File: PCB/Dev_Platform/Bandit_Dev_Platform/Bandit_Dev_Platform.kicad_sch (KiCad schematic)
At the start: 136 parts, among them J1 Conn_01x03_Pin, J10 Conn_01x05_Pin, J11 Conn_01x05_Pin, J2 SMA, J3 Conn_01x05_Pin, J4 Conn_01x05_Pin, J5 BNC, J6 BNC, J7 SMA, J8 Conn_01x05_Pin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

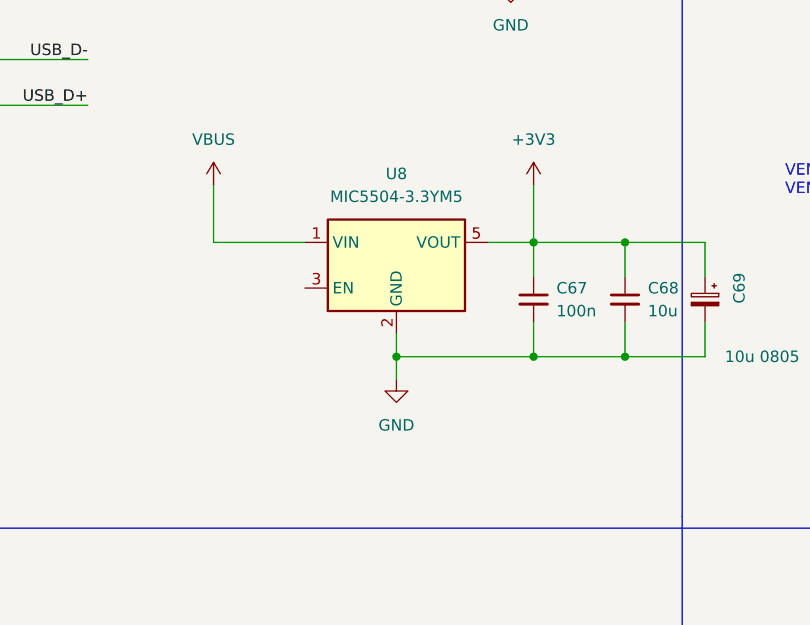
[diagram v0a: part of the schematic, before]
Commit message: Fixed BNC issue, changed more parts to be free.99
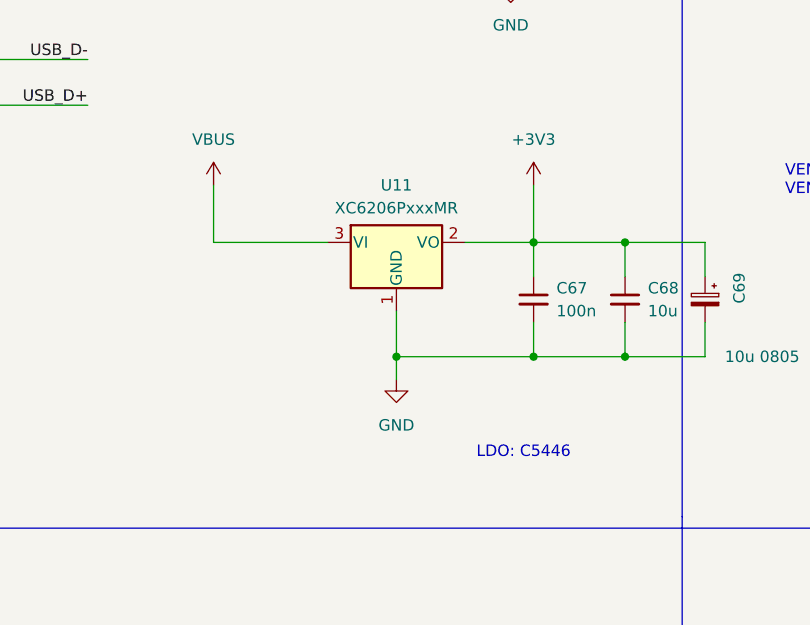
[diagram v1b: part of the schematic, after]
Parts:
- removed U8: MIC5504-3.3YM5, Package_TO_SOT_SMD:SOT-23-5, symbol Regulator_Linear:MIC5504-3.3YM5
- added U11: XC6206PxxxMR, Package_TO_SOT_SMD:SOT-23-3, symbol Regulator_Linear:XC6206PxxxMR
- J5, J6: footprint ADS8584SIPM:BNC_THT -> BANDIT_PCB_Lib:DOSIN-801-0050
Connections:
- net +3V3: now also U11.2 (VO)
- net GND: now also U11.1 (GND)
- net VBUS: now also U11.3 (VI)
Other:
- note added: "LDO: C5446"
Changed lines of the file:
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@@
     (stroke (width 0) (type default))
   )
+  (wire (pts (xy 133.35 80.01) (xy 140.97 80.01))
+    (stroke (width 0) (type default))
+  )
   (wire (pts (xy 382.27 298.45) (xy 382.27 306.07))
     (stroke (width 0) (type default))
@@
     (stroke (width 0) (type default))
   )
-  (wire (pts (xy 125.73 90.17) (xy 125.73 92.71))
+  (wire (pts (xy 125.73 87.63) (xy 125.73 92.71))
     (stroke (width 0) (type default))
   )
@@
     (stroke (width 0) (type default))
   )
-  (wire (pts (xy 105.41 80.01) (xy 115.57 80.01))
+  (wire (pts (xy 105.41 80.01) (xy 118.11 80.01))
     (stroke (width 0) (type default))
   )
@@
     (stroke (width 0) (type default))
   )
-  (wire (pts (xy 140.97 80.01) (xy 135.89 80.01))
-    (stroke (width 0) (type default))
-  )
   (wire (pts (xy 95.25 218.44) (xy 114.3 218.44))
     (stroke (width 0) (type default))
@@
     (effects (font (size 4 4) bold) (justify left bottom))
   )
+  (text "LDO: C5446" (at 134.62 104.14 0)
+    (effects (font (size 1.27 1.27)) (justify left bottom))
+  )
   (text "220p + 100p = 320p" (at 330.2 326.39 0)
     (effects (font (size 1.27 1.27)) (justify left bottom))
@@
       (effects (font (size 1.27 1.27)) (justify left))
     )
-    (property "Footprint" "ADS8584SIPM:BNC_THT" (at 553.72 69.85 0)
+    (property "Footprint" "BANDIT_PCB_Lib:DOSIN-801-0050" (at 553.72 69.85 0)
       (effects (font (size 1.27 1.27)) hide)
     )
@@
     )
   )
-  (symbol (lib_id "Regulator_Linear:MIC5504-3.3YM5") (at 125.73 82.55 0) (unit 1)
-    (in_bom yes) (on_board yes) (dnp no) (fields_autoplaced)
-    (property "Reference" "U8" (at 125.73 72.39 0)
-      (effects (font (size 1.27 1.27)))
-    )
-    (property "Value" "MIC5504-3.3YM5" (at 125.73 74.93 0)
-      (effects (font (size 1.27 1.27)))
-    )
-    (property "Footprint" "Package_TO_SOT_SMD:SOT-23-5" (at 125.73 92.71 0)
-      (effects (font (size 1.27 1.27)) hide)
-    )
-    (property "Datasheet" "http://ww1.microchip.com/downloads/en/DeviceDoc/MIC550X.pdf" (at 119.38 76.2 0)
-      (effects (font (size 1.27 1.27)) hide)
-    )
-    (pin "1")
-    (pin "2")
-    (pin "3")
-    (pin "4")
-    (pin "5")
-    (instances
-      (project "Bandit_Dev_Platform"
-        (path "/dd3bbd79-e9c1-4976-be4e-f98731bec367"
-          (reference "U8") (unit 1)
-        )
-      )
-    )
-  )
   (symbol (lib_id "power:GNDA") (at 388.62 231.14 0) (mirror x) (unit 1)
     (in_bom yes) (on_board yes) (dnp no) (fields_autoplaced)
@@
     )
   )
+  (symbol (lib_id "Regulator_Linear:XC6206PxxxMR") (at 125.73 80.01 0) (unit 1)
+    (in_bom yes) (on_board yes) (dnp no) (fields_autoplaced)
+    (property "Reference" "U11" (at 125.73 73.66 0)
+      (effects (font (size 1.27 1.27)))
+    )
+    (property "Value" "XC6206PxxxMR" (at 125.73 76.2 0)
+      (effects (font (size 1.27 1.27)))
+    )
+    (property "Footprint" "Package_TO_SOT_SMD:SOT-23-3" (at 125.73 74.295 0)
+      (effects (font (size 1.27 1.27) italic) hide)
+    )
+    (property "Datasheet" "https://www.torexsemi.com/file/xc6206/XC6206.pdf" (at 125.73 80.01 0)
+      (effects (font (size 1.27 1.27)) hide)
+    )
+    (pin "1")
+    (pin "2")
+    (pin "3")
+    (instances
+      (project "Bandit_Dev_Platform"
+        (path "/dd3bbd79-e9c1-4976-be4e-f98731bec367"
+          (reference "U11") (unit 1)
+        )
+      )
+    )
+  )
   (symbol (lib_id "Device:C_Small") (at 478.79 151.13 0) (unit 1)
     (in_bom yes) (on_board yes) (dnp no)
@@
       (effects (font (size 1.27 1.27)) (justify left))
     )
-    (property "Footprint" "ADS8584SIPM:BNC_THT" (at 553.72 151.13 0)
+    (property "Footprint" "BANDIT_PCB_Lib:DOSIN-801-0050" (at 553.72 151.13 0)
       (effects (font (size 1.27 1.27)) hide)
     )

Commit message: Done?
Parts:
- added C72, C73: 10u 0805, Capacitor_SMD:C_0805_2012Metric, symbol Device:C_Polarized_Small
- added C74: 100n, Capacitor_SMD:C_0402_1005Metric, symbol Device:C_Small
- added J12: Conn_01x02_Pin, Connector_PinSocket_2.54mm:PinSocket_1x02_P2.54mm_Vertical, symbol Connector:Conn_01x02_Pin
- added R13, R15: 51k, Resistor_SMD:R_0402_1005Metric, symbol Device:R_Small_US
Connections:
- net +3V3: now also C74.1
- net GND: now also C74.2, R15.2
- net VDDA: now also R13.1
- net WGN_OUT: now also C73.2, J12.2 (Pin_2); no longer J6.1 (In), J7.1 (In), R7.1, U7.3 (CH1)
- new net WGN_OUT_PORT: C72.1, C73.1, J12.1 (Pin_1), J6.1 (In), J7.1 (In)
- new net WGN_PGA_IN: C72.2, R13.2, R15.1, R7.1, U7.3 (CH1)
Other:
- moved on the sheet: C25, J2, J5, J6, J7, R25, R26

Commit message: More done
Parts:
- added C75: 100n, Capacitor_SMD:C_0402_1005Metric, symbol Device:C_Small
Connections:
- net +3V3: now also C75.1
- net GND: now also C75.2
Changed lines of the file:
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@@
   (junction (at 488.95 238.76) (diameter 0) (color 0 0 0 0)
   )
+  (junction (at 7.62 170.18) (diameter 0) (color 0 0 0 0)
+  )
   (junction (at 31.75 287.02) (diameter 0) (color 0 0 0 0)
   )
@@
   (junction (at 245.11 265.43) (diameter 0) (color 0 0 0 0)
   )
+  (junction (at 7.62 179.07) (diameter 0) (color 0 0 0 0)
+  )
   (junction (at 271.78 72.39) (diameter 0) (color 0 0 0 0)
   )
@@
     (stroke (width 0) (type default))
   )
+  (wire (pts (xy -2.54 171.45) (xy -2.54 170.18))
+    (stroke (width 0) (type default))
+  )
   (wire (pts (xy 434.34 288.29) (xy 438.15 288.29))
     (stroke (width 0) (type default))
@@
     (stroke (width 0) (type default))
   )
+  (wire (pts (xy -2.54 170.18) (xy 7.62 170.18))
+    (stroke (width 0) (type default))
+  )
   (wire (pts (xy 97.79 33.02) (xy 97.79 34.29))
     (stroke (width 0) (type default))
@@
     (stroke (width 0) (type default))
   )
+  (wire (pts (xy -2.54 179.07) (xy -2.54 176.53))
+    (stroke (width 0) (type default))
+  )
   (wire (pts (xy 176.53 132.08) (xy 176.53 133.35))
     (stroke (width 0) (type default))
@@
     (stroke (width 0) (type default))
   )
+  (wire (pts (xy 7.62 179.07) (xy -2.54 179.07))
+    (stroke (width 0) (type default))
+  )
   (wire (pts (xy 106.68 284.48) (xy 106.68 279.4))
     (stroke (width 0) (type default))
@@
         )
       )
+    )
+  )
+  (symbol (lib_id "Device:C_Small") (at -2.54 173.99 0) (mirror y) (unit 1)
+    (in_bom yes) (on_board yes) (dnp no)
+    (property "Reference" "C75" (at -5.08 172.7263 0)
+      (effects (font (size 1.27 1.27)) (justify left))
+    )
+    (property "Value" "100n" (at -5.08 175.2663 0)
+      (effects (font (size 1.27 1.27)) (justify left))
+    )
+    (property "Footprint" "Capacitor_SMD:C_0402_1005Metric" (at -2.54 173.99 0)
+      (effects (font (size 1.27 1.27)) hide)
+    )
+    (property "Datasheet" "~" (at -2.54 173.99 0)
+      (effects (font (size 1.27 1.27)) hide)
+    )
+    (pin "1")
+    (pin "2")
+    (instances
+      (project "Bandit_Dev_Platform"
+        (path "/dd3bbd79-e9c1-4976-be4e-f98731bec367"
+          (reference "C75") (unit 1)
+        )
+      )

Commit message: Schematic cleanup
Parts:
- removed C12, C15, C17, C3, C75: 100n, Capacitor_SMD:C_0402_1005Metric, symbol Device:C_Small
- removed C18: 10n, Capacitor_SMD:C_0402_1005Metric, symbol Device:C_Small
- removed C2: 1u, Capacitor_SMD:C_0402_1005Metric, symbol Device:C_Small
- removed C70: 10u 0805, Capacitor_SMD:C_0805_2012Metric, symbol Device:C_Polarized_Small
- removed J10, J11, J3, J4: Conn_01x05_Pin, Connector_PinHeader_2.54mm:PinHeader_1x05_P2.54mm_Vertical, symbol Connector:Conn_01x05_Pin
- removed J2: SMA, Capacitor_SMD:C_0402_1005Metric, symbol Connector:Conn_Coaxial
- removed J7: SMA, symbol Connector:Conn_Coaxial
- removed JP3: SolderJumper_2_Open, Jumper:SolderJumper-2_P1.3mm_Open_TrianglePad1.0x1.5mm, symbol Jumper:SolderJumper_2_Open
- removed U3: AP2210N-4.0TRG1, Package_TO_SOT_SMD:SOT-23-3, symbol BANDIT_PCB_Lib:AP2210N-4.0TRG1
- removed X1: SG-210STF, Oscillator:Oscillator_SMD_SeikoEpson_SG210-4Pin_2.5x2.0mm, symbol Oscillator:SG-210STF
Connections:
- no-connect marks 5 -> 4
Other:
- note added: "WGN Output AC Coupling Selection"
- note removed: "DO NOT INCLUDE!!"
- note removed: "FOR CLIPPY OPTION"

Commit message: Dev platform and Filter Test pcb polished, ordered
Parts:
- removed J1: Conn_01x03_Pin, Connector_PinHeader_2.54mm:PinHeader_1x03_P2.54mm_Vertical, symbol Connector:Conn_01x03_Pin
- removed J8: Conn_01x05_Pin, Connector_PinHeader_2.54mm:PinHeader_1x05_P2.54mm_Vertical, symbol Connector:Conn_01x05_Pin
- removed J9: Conn_01x06_Pin, Connector_PinHeader_2.54mm:PinHeader_1x05_P2.54mm_Vertical, symbol Connector:Conn_01x06_Pin
- removed JP1, JP2: SolderJumper_2_Open, Jumper:SolderJumper-2_P1.3mm_Open_TrianglePad1.0x1.5mm, symbol Jumper:SolderJumper_2_Open
- added C12, C15, C3: 100n, Capacitor_SMD:C_0402_1005Metric, symbol Device:C_Small
- added C17, C18, C2: 10u, Capacitor_SMD:C_0402_1005Metric, symbol Device:C_Small
- added C70: 2u2, Capacitor_SMD:C_0402_1005Metric, symbol Device:C_Small
- added R16, R17, R18, R19, R20, R42: 10k, Resistor_SMD:R_0402_1005Metric, symbol Device:R_Small_US
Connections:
- net +3V3: now also C70.1
- net GND: now also C12.2, C15.2, C3.2, C70.2, R17.2, R19.2, R42.2
- net SE_SIG_A: now also C18.2; no longer R22.1
- net SE_SIG_B: now also C17.2; no longer R23.1
- net SIG_IN: now also C2.1, R16.2, R17.1; no longer U7.1 (VOUT)
- net VDDA: now also C12.1, C15.1, C3.1, R16.1, R18.1, R20.1
- net VDDA_EN: now also R7.2, U2.32 (GPIO21), U4.3 (EN)
- new net: C18.1, R20.2, R22.1, R42.1
- new net: C17.1, R18.2, R19.1, R23.1
- new net: C2.2, U7.1 (VOUT)
- no-connect marks 4 -> 14

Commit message: Need to update fab, but fixed C70 duplicate issue from version mismatch
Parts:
- added C75: 10u 0805, Capacitor_SMD:C_0805_2012Metric, symbol Device:C_Polarized_Small
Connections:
- net GND: now also C75.2
- net VBUS: now also C75.1
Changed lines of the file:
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@@
   (junction (at 505.46 57.15) (diameter 0) (color 0 0 0 0)
   )
+  (junction (at 222.25 63.5) (diameter 0) (color 0 0 0 0)
+  )
   (junction (at 438.15 288.29) (diameter 0) (color 0 0 0 0)
   )
@@
     (stroke (width 0) (type default))
   )
+  (wire (pts (xy 210.82 64.77) (xy 210.82 63.5))
+    (stroke (width 0) (type default))
+  )
   (wire (pts (xy 392.43 293.37) (xy 388.62 293.37))
     (stroke (width 0) (type default))
@@
     (stroke (width 0) (type default))
   )
+  (wire (pts (xy 210.82 63.5) (xy 222.25 63.5))
+    (stroke (width 0) (type default))
+  )
   (wire (pts (xy 361.95 295.91) (xy 361.95 292.1))
     (stroke (width 0) (type default))
@@
     (stroke (width 0) (type default))
   )
+  (wire (pts (xy 222.25 63.5) (xy 222.25 72.39))
+    (stroke (width 0) (type default))
+  )
   (wire (pts (xy 532.13 153.67) (xy 532.13 156.21))
     (stroke (width 0) (type default))
@@
     (stroke (width 0) (type default))
   )
-  (wire (pts (xy 222.25 62.23) (xy 222.25 72.39))
+  (wire (pts (xy 222.25 62.23) (xy 222.25 63.5))
     (stroke (width 0) (type default))
   )
@@
     )
   )
+  (symbol (lib_id "power:GND") (at 210.82 69.85 0) (unit 1)
+    (in_bom yes) (on_board yes) (dnp no) (fields_autoplaced)
+    (property "Reference" "#PWR057" (at 210.82 76.2 0)
+      (effects (font (size 1.27 1.27)) hide)
+    )
+    (property "Value" "GND" (at 210.82 74.93 0)
+      (effects (font (size 1.27 1.27)))
+    )
+    (property "Footprint" "" (at 210.82 69.85 0)
+      (effects (font (size 1.27 1.27)) hide)
+    )
+    (property "Datasheet" "" (at 210.82 69.85 0)
+      (effects (font (size 1.27 1.27)) hide)
+    )
+    (pin "1")
+    (instances
+      (project "Bandit_Dev_Platform"
+        (path "/dd3bbd79-e9c1-4976-be4e-f98731bec367"
+          (reference "#PWR057") (unit 1)
+        )
+      )
+    )
+  )
   (symbol (lib_id "Device:C_Small") (at 510.54 60.96 0) (unit 1)
     (in_bom yes) (on_board yes) (dnp no) (fields_autoplaced)
@@
         )
       )
+    )
+  )
+  (symbol (lib_id "Device:C_Polarized_Small") (at 210.82 67.31 0) (mirror y) (unit 1)
+    (in_bom yes) (on_board yes) (dnp no)
+    (property "Reference" "C75" (at 214.63 66.04 90)
+      (effects (font (size 1.27 1.27)))
+    )
+    (property "Value" "10u 0805" (at 217.17 73.66 0)
+      (effects (font (size 1.27 1.27)))
+    )
+    (property "Footprint" "Capacitor_SMD:C_0805_2012Metric" (at 210.82 67.31 0)
+      (effects (font (size 1.27 1.27)) hide)
+    )
+    (property "Datasheet" "~" (at 210.82 67.31 0)
+      (effects (font (size 1.27 1.27)) hide)
+    )
+    (pin "1")
+    (pin "2")
+    (instances
+      (project "Bandit_Dev_Platform"
+        (path "/dd3bbd79-e9c1-4976-be4e-f98731bec367"
+          (reference "C75") (unit 1)
+        )
+      )

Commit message: Added Bandit_Pins header, RUN pin wasn't tied high.. hopefully wont be an issue lol
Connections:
- net +3V3: now also U2.26 (RUN)
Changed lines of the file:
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@@
     (stroke (width 0) (type default))
   )
+  (wire (pts (xy 31.75 210.82) (xy 44.45 210.82))
+    (stroke (width 0) (type default))
+  )
   (wire (pts (xy 138.43 50.8) (xy 138.43 46.99))
     (stroke (width 0) (type default))
@@
     (stroke (width 0) (type default))
   )
+  (wire (pts (xy 31.75 208.28) (xy 31.75 210.82))
+    (stroke (width 0) (type default))
+  )
   (wire (pts (xy 288.29 74.93) (xy 288.29 72.39))
     (stroke (width 0) (type default))
@@
         )
       )
+    )
+  )
+  (symbol (lib_id "power:+3V3") (at 31.75 208.28 0) (unit 1)
+    (in_bom yes) (on_board yes) (dnp no) (fields_autoplaced)
+    (property "Reference" "#PWR058" (at 31.75 212.09 0)
+      (effects (font (size 1.27 1.27)) hide)
+    )
+    (property "Value" "+3V3" (at 31.75 203.2 0)
+      (effects (font (size 1.27 1.27)))
+    )
+    (property "Footprint" "" (at 31.75 208.28 0)
+      (effects (font (size 1.27 1.27)) hide)
+    )
+    (property "Datasheet" "" (at 31.75 208.28 0)
+      (effects (font (size 1.27 1.27)) hide)
+    )
+    (pin "1")
+    (instances
+      (project "Bandit_Dev_Platform"
+        (path "/dd3bbd79-e9c1-4976-be4e-f98731bec367"
+          (reference "#PWR058") (unit 1)
+        )
+      )
